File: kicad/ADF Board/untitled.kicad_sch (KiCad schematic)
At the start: 12 parts, among them J4 I2C_JST-PH_STEMMA, J5 I2C_JST-PH_STEMMA, U1 xiao_esp32s3

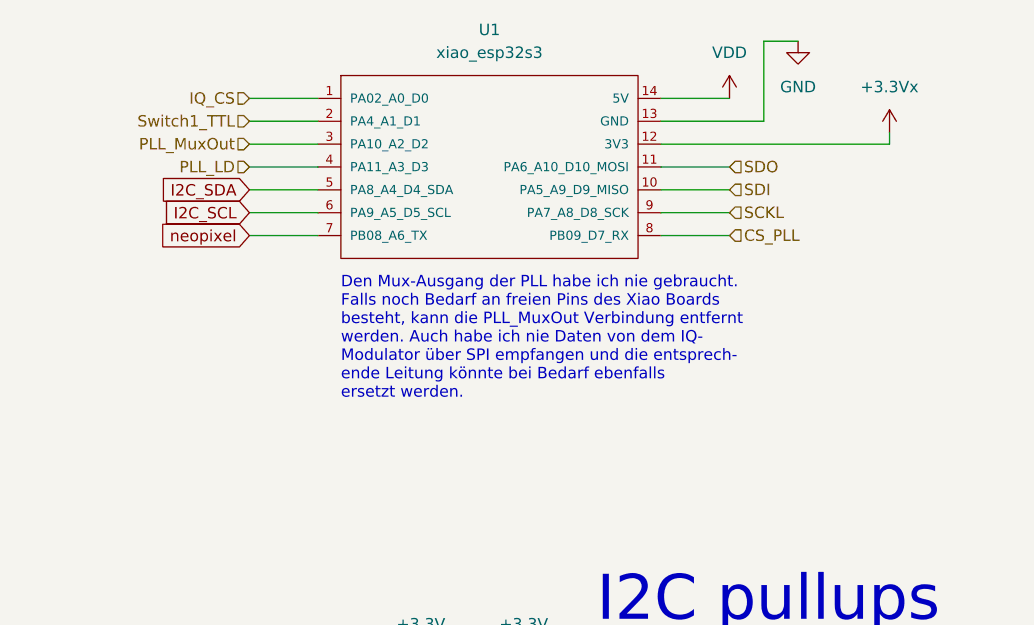
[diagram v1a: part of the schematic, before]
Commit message: Started parts selection for assemblability Considering deleting the I/Q modulator and periphery
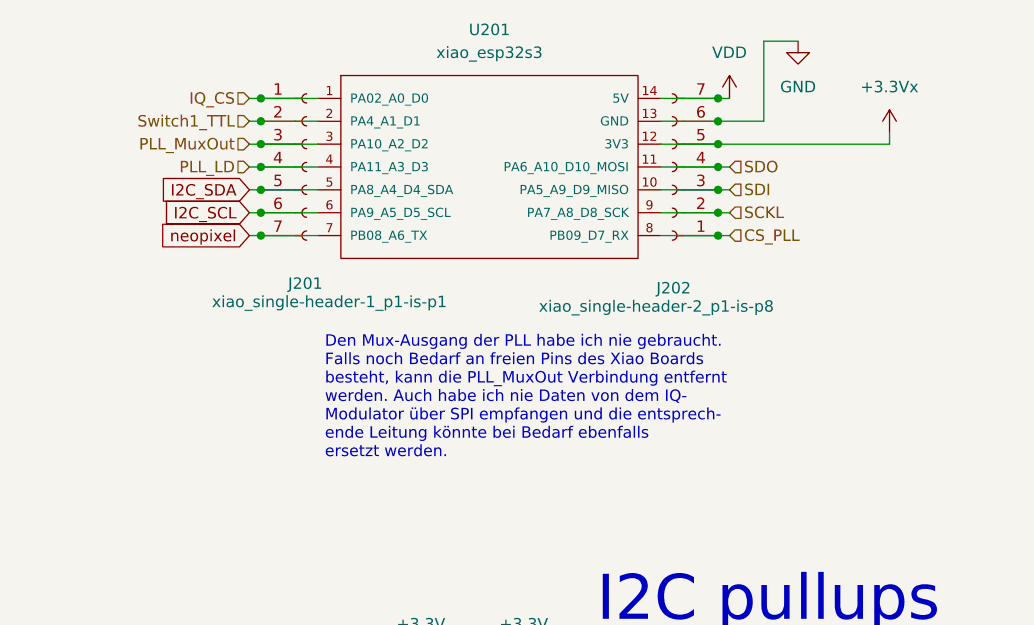
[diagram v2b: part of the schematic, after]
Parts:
- removed U1: xiao_esp32s3, SamacSys_Parts:XIAO-ESP32S3-DIP, symbol xiao-esp32s3_lib:xiao_esp32s3
- added J201: xiao_single-header-1_p1-is-p1, Connector_PinSocket_2.54mm:PinSocket_1x07_P2.54mm_Vertical, symbol Connector:Conn_01x07_Socket
- added J202: xiao_single-header-2_p1-is-p8, Connector_PinSocket_2.54mm:PinSocket_1x07_P2.54mm_Vertical, symbol Connector:Conn_01x07_Socket
- added U201: xiao_esp32s3, lib:XIAO-Generic-Thruhole-14P-2.54-21X17.8MM, symbol xiao-esp32s3_lib:xiao_esp32s3
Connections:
- net +3.3Vx: now also J202.5 (Pin_5), U201.12 (3V3)
- net CS_PLL: now also J202.1 (Pin_1), U201.8 (PB09_D7_RX)
- net GND: now also J202.6 (Pin_6), U201.13 (GND)
- net I2C_SCL: now also J201.6 (Pin_6), U201.6 (PA9_A5_D5_SCL)
- net I2C_SDA: now also J201.5 (Pin_5), U201.5 (PA8_A4_D4_SDA)
- net IQ_CS: now also J201.1 (Pin_1), U201.1 (PA02_A0_D0)
- net PLL_LD: now also J201.4 (Pin_4), U201.4 (PA11_A3_D3)
- net PLL_MuxOut: now also J201.3 (Pin_3), U201.3 (PA10_A2_D2)
- net SCKL: now also J202.2 (Pin_2), U201.9 (PA7_A8_D8_SCK)
- net SDI: now also J202.3 (Pin_3), U201.10 (PA5_A9_D9_MISO)
- net SDO: now also J202.4 (Pin_4), U201.11 (PA6_A10_D10_MOSI)
- net Switch1_TTL: now also J201.2 (Pin_2), U201.2 (PA4_A1_D1)
- net VDD: now also J202.7 (Pin_7), U201.14 (5V)
- net neopixel: now also J201.7 (Pin_7), U201.7 (PB08_A6_TX)

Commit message: Deleted I/Q mod, switch, charge pump Found candidates for RF amp and PLL
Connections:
- net IQ_CS: no longer names the net of J201.1 (Pin_1), U201.1 (PA02_A0_D0)
- net Switch1_TTL: no longer names the net of J201.2 (Pin_2), U201.2 (PA4_A1_D1)
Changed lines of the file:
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@@
-		)
-	)
-	(hierarchical_label "IQ_CS"
-		(shape input)
-		(at 115.57 22.86 180)
-		(effects
-			(font
-				(size 1.27 1.27)
-			)
-			(justify right)
-		)
-	)
-	(hierarchical_label "Switch1_TTL"
-		(shape input)
-		(at 115.57 25.4 180)
-		(effects
-			(font
-				(size 1.27 1.27)
-			)
-			(justify right)
 		)
 	)
